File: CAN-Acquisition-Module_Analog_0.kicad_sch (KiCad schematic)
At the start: 23 parts, among them J8 OSTVN04A150, J9 OSTVN04A150, U6 BD12734FVJ-E2

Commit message: BOM updated for LCSC. Still a WIP.
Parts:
- J8, J9: LCSC (none) -> C708735; Mfr. On Shore Technology -> On-Shore
- R29, R30, R31, R32: LCSC (none) -> C351551
- R33, R34, R35, R36: Tolerance (none) -> 1%
- U6: Alternate P/N (none) -> MCP6L04T; LCSC (none) -> C49038
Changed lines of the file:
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@@
+      (effects (font (size 1.27 1.27)) hide)
+    )
+    (property "LCSC" "C351551" (id 7) (at 64.77 88.9 0)
       (effects (font (size 1.27 1.27)) hide)
     )
@@
     )
     (property "P/N" "ERA-6AEB622V" (id 6) (at 64.77 24.13 0)
+      (effects (font (size 1.27 1.27)) hide)
+    )
+    (property "LCSC" "C351551" (id 7) (at 64.77 24.13 0)
       (effects (font (size 1.27 1.27)) hide)
     )
@@
     )
     (property "P/N" "BD12734FVJ-E2" (id 5) (at 168.91 137.16 0)
+      (effects (font (size 1.27 1.27)) hide)
+    )
+    (property "Alternate P/N" "MCP6L04T" (id 6) (at 168.91 137.16 0)
+      (effects (font (size 1.27 1.27)) hide)
+    )
+    (property "LCSC" "C49038" (id 7) (at 168.91 137.16 0)
       (effects (font (size 1.27 1.27)) hide)
     )
@@
       (effects (font (size 1.27 1.27)) hide)
     )
-    (property "Mfr." "On Shore Technology" (id 5) (at 43.18 34.29 0)
+    (property "Mfr." "On-Shore" (id 5) (at 43.18 34.29 0)
+      (effects (font (size 1.27 1.27)) hide)
+    )
+    (property "LCSC" "C708735" (id 6) (at 43.18 34.29 0)
       (effects (font (size 1.27 1.27)) hide)
     )
@@
       (effects (font (size 1.27 1.27)) hide)
     )
-    (property "Mfr." "On Shore Technology" (id 5) (at 43.18 99.06 0)
+    (property "Mfr." "On-Shore" (id 5) (at 43.18 99.06 0)
+      (effects (font (size 1.27 1.27)) hide)
+    )
+    (property "LCSC" "C708735" (id 6) (at 43.18 99.06 0)
       (effects (font (size 1.27 1.27)) hide)
     )
@@
     )
     (property "P/N" "BD12734FVJ-E2" (id 5) (at 52.07 173.99 0)
+      (effects (font (size 1.27 1.27)) hide)
+    )
+    (property "Alternate P/N" "MCP6L04T" (id 6) (at 52.07 173.99 0)
+      (effects (font (size 1.27 1.27)) hide)
+    )
+    (property "LCSC" "C49038" (id 7) (at 52.07 173.99 0)
       (effects (font (size 1.27 1.27)) hide)
     )
@@
       (effects (font (size 1.27 1.27)) hide)
     )
+    (property "Alternate P/N" "MCP6L04T" (id 6) (at 168.91 69.85 0)
+      (effects (font (size 1.27 1.27)) hide)
+    )
+    (property "LCSC" "C49038" (id 7) (at 168.91 69.85 0)
+      (effects (font (size 1.27 1.27)) hide)
+    )
     (pin "1")
     (pin "2")
@@
       (effects (font (size 1.27 1.27)) hide)
     )
+    (property "Tolerance" "1%" (id 6) (at 148.59 31.75 0)
+      (effects (font (size 1.27 1.27)) hide)
+    )
     (pin "1")
     (pin "2")
@@
     )
     (property "P/N" "BD12734FVJ-E2" (id 5) (at 168.91 99.06 0)
+      (effects (font (size 1.27 1.27)) hide)
+    )
+    (property "Alternate P/N" "MCP6L04T" (id 6) (at 168.91 99.06 0)
+      (effects (font (size 1.27 1.27)) hide)
+    )
+    (property "LCSC" "C49038" (id 7) (at 168.91 99.06 0)
       (effects (font (size 1.27 1.27)) hide)
     )
@@
       (effects (font (size 1.27 1.27)) hide)
     )
+    (property "Tolerance" "1%" (id 6) (at 153.67 96.52 0)
+      (effects (font (size 1.27 1.27)) hide)
+    )
     (pin "1")
     (pin "2")
@@
     )
     (property "P/N" "ERA-6AEB622V" (id 6) (at 74.93 24.13 0)
+      (effects (font (size 1.27 1.27)) hide)
+    )
+    (property "LCSC" "C351551" (id 7) (at 74.93 24.13 0)
       (effects (font (size 1.27 1.27)) hide)
     )
@@
     )
     (property "P/N" "BD12734FVJ-E2" (id 5) (at 168.91 34.29 0)
+      (effects (font (size 1.27 1.27)) hide)
+    )
+    (property "Alternate P/N" "MCP6L04T" (id 6) (at 168.91 34.29 0)
+      (effects (font (size 1.27 1.27)) hide)
+    )
+    (property "LCSC" "C49038" (id 7) (at 168.91 34.29 0)
       (effects (font (size 1.27 1.27)) hide)
     )
@@
       (effects (font (size 1.27 1.27)) hide)
     )
+    (property "LCSC" "C351551" (id 7) (at 74.93 88.9 0)
+      (effects (font (size 1.27 1.27)) hide)
+    )
     (pin "1")
     (pin "2")
@@
       (effects (font (size 1.27 1.27)) hide)
     )
+    (property "Tolerance" "1%" (id 6) (at 144.78 101.6 0)
+      (effects (font (size 1.27 1.27)) hide)
+    )
     (pin "1")
     (pin "2")
@@
       (effects (font (size 1.27 1.27)) hide)
     )
+    (property "Tolerance" "1%" (id 6) (at 142.24 36.83 0)
+      (effects (font (size 1.27 1.27)) hide)
+    )

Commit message: BOM updated for LCSC. Still a WIP
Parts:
- D15, D16, D17, D18: LCSC (none) -> C558429
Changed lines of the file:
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@@
+      (effects (font (size 1.27 1.27)) hide)
+    )
+    (property "LCSC" "C558429" (id 6) (at 77.47 114.3 0)
       (effects (font (size 1.27 1.27)) hide)
     )
@@
     )
     (property "P/N" "D1213A-01SO-7" (id 5) (at 77.47 49.53 0)
+      (effects (font (size 1.27 1.27)) hide)
+    )
+    (property "LCSC" "C558429" (id 6) (at 77.47 49.53 0)
       (effects (font (size 1.27 1.27)) hide)
     )
@@
       (effects (font (size 1.27 1.27)) hide)
     )
+    (property "LCSC" "C558429" (id 6) (at 64.77 49.53 0)
+      (effects (font (size 1.27 1.27)) hide)
+    )
     (pin "1")
     (pin "2")
@@
       (effects (font (size 1.27 1.27)) hide)
     )
+    (property "LCSC" "C558429" (id 6) (at 64.77 114.3 0)
+      (effects (font (size 1.27 1.27)) hide)
+    )

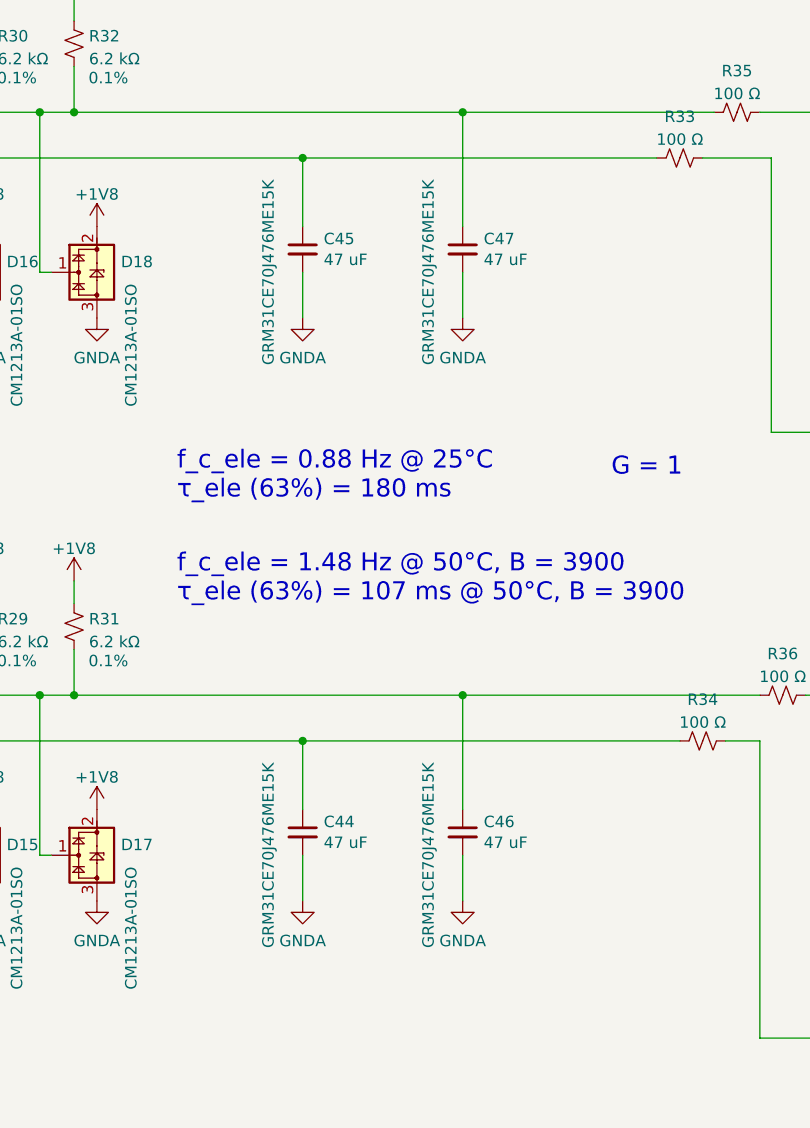
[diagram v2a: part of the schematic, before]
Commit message: Changed 47uF cap to 4.7uF
Filtration can be done in software instead of hardware
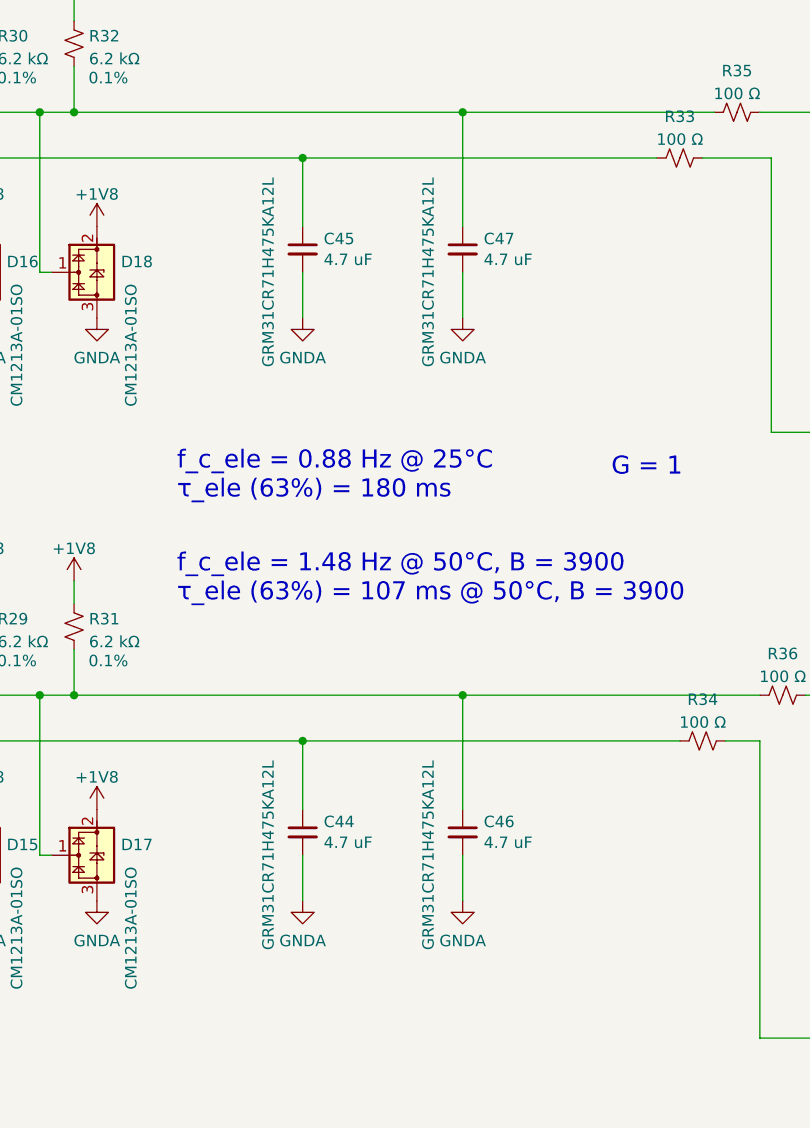
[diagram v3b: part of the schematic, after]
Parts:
- C44, C45, C46, C47: value 47 uF -> 4.7 uF; Mfr. Murata -> Murata Electronics; P/N GRM31CE70J476ME15K -> GRM31CR71H475KA12L; Rated Voltage (none) -> 50V
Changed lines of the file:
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@@
       (effects (font (size 1.27 1.27)) (justify left))
     )
-    (property "Value" "47 uF" (id 1) (at 120.4468 112.903 0)
+    (property "Value" "4.7 uF" (id 1) (at 120.4468 112.903 0)
       (effects (font (size 1.27 1.27)) (justify left))
     )
@@
       (effects (font (size 1.27 1.27)) hide)
     )
-    (property "Datasheet" "https://search.murata.co.jp/Ceramy/image/img/A01X/G101/ENG/GRM31CE70J476ME15-01.pdf" (id 3) (at 118.11 111.76 0)
-      (effects (font (size 1.27 1.27)) hide)
-    )
-    (property "P/N" "GRM31CE70J476ME15K" (id 4) (at 114.3 114.3 90))
-    (property "Mfr." "Murata" (id 5) (at 118.11 111.76 0)
+    (property "Datasheet" "https://search.murata.co.jp/Ceramy/image/img/A01X/G101/ENG/GRM31CR71H475KA12-01.pdf" (id 3) (at 118.11 111.76 0)
+      (effects (font (size 1.27 1.27)) hide)
+    )
+    (property "P/N" "GRM31CR71H475KA12L" (id 4) (at 114.3 114.3 90))
+    (property "Mfr." "Murata Electronics" (id 5) (at 118.11 111.76 0)
+      (effects (font (size 1.27 1.27)) hide)
+    )
+    (property "Rated Voltage" "50V" (id 6) (at 118.11 111.76 0)
       (effects (font (size 1.27 1.27)) hide)
     )
@@
       (effects (font (size 1.27 1.27)) (justify left))
     )
-    (property "Value" "47 uF" (id 1) (at 102.6668 112.903 0)
+    (property "Value" "4.7 uF" (id 1) (at 102.6668 112.903 0)
       (effects (font (size 1.27 1.27)) (justify left))
     )
@@
       (effects (font (size 1.27 1.27)) hide)
     )
-    (property "Datasheet" "https://search.murata.co.jp/Ceramy/image/img/A01X/G101/ENG/GRM31CE70J476ME15-01.pdf" (id 3) (at 100.33 111.76 0)
-      (effects (font (size 1.27 1.27)) hide)
-    )
-    (property "P/N" "GRM31CE70J476ME15K" (id 4) (at 96.52 114.3 90))
-    (property "Mfr." "Murata" (id 5) (at 100.33 111.76 0)
+    (property "Datasheet" "https://search.murata.co.jp/Ceramy/image/img/A01X/G101/ENG/GRM31CR71H475KA12-01.pdf" (id 3) (at 100.33 111.76 0)
+      (effects (font (size 1.27 1.27)) hide)
+    )
+    (property "P/N" "GRM31CR71H475KA12L" (id 4) (at 96.52 114.3 90))
+    (property "Mfr." "Murata Electronics" (id 5) (at 100.33 111.76 0)
+      (effects (font (size 1.27 1.27)) hide)
+    )
+    (property "Rated Voltage" "50V" (id 6) (at 100.33 111.76 0)
       (effects (font (size 1.27 1.27)) hide)
     )
@@
       (effects (font (size 1.27 1.27)) (justify left))
     )
-    (property "Value" "47 uF" (id 1) (at 120.4468 48.133 0)
+    (property "Value" "4.7 uF" (id 1) (at 120.4468 48.133 0)
       (effects (font (size 1.27 1.27)) (justify left))
     )
@@
       (effects (font (size 1.27 1.27)) hide)
     )
-    (property "Datasheet" "https://search.murata.co.jp/Ceramy/image/img/A01X/G101/ENG/GRM31CE70J476ME15-01.pdf" (id 3) (at 118.11 46.99 0)
-      (effects (font (size 1.27 1.27)) hide)
-    )
-    (property "P/N" "GRM31CE70J476ME15K" (id 4) (at 114.3 49.53 90))
-    (property "Mfr." "Murata" (id 5) (at 118.11 46.99 0)
+    (property "Datasheet" "https://search.murata.co.jp/Ceramy/image/img/A01X/G101/ENG/GRM31CR71H475KA12-01.pdf" (id 3) (at 118.11 46.99 0)
+      (effects (font (size 1.27 1.27)) hide)
+    )
+    (property "P/N" "GRM31CR71H475KA12L" (id 4) (at 114.3 49.53 90))
+    (property "Mfr." "Murata Electronics" (id 5) (at 118.11 46.99 0)
+      (effects (font (size 1.27 1.27)) hide)
+    )
+    (property "Rated Voltage" "50V" (id 6) (at 118.11 46.99 0)
       (effects (font (size 1.27 1.27)) hide)
     )
@@
       (effects (font (size 1.27 1.27)) (justify left))
     )
-    (property "Value" "47 uF" (id 1) (at 102.6668 48.133 0)
+    (property "Value" "4.7 uF" (id 1) (at 102.6668 48.133 0)
       (effects (font (size 1.27 1.27)) (justify left))
     )
@@
       (effects (font (size 1.27 1.27)) hide)
     )
-    (property "Datasheet" "https://search.murata.co.jp/Ceramy/image/img/A01X/G101/ENG/GRM31CE70J476ME15-01.pdf" (id 3) (at 100.33 46.99 0)
-      (effects (font (size 1.27 1.27)) hide)
-    )
-    (property "P/N" "GRM31CE70J476ME15K" (id 4) (at 96.52 49.53 90))
-    (property "Mfr." "Murata" (id 5) (at 100.33 46.99 0)
-      (effects (font (size 1.27 1.27)) hide)
-    )
+    (property "Datasheet" "https://search.murata.co.jp/Ceramy/image/img/A01X/G101/ENG/GRM31CR71H475KA12-01.pdf" (id 3) (at 100.33 46.99 0)
+      (effects (font (size 1.27 1.27)) hide)
+    )
+    (property "P/N" "GRM31CR71H475KA12L" (id 4) (at 96.52 49.53 90))
+    (property "Mfr." "Murata Electronics" (id 5) (at 100.33 46.99 0)
+      (effects (font (size 1.27 1.27)) hide)
+    )
+    (property "Rated Voltage" "50V" (id 6) (at 100.33 46.99 0)
+      (effects (font (size 1.27 1.27)) hide)
+    )

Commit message: Created Rev B1
Replaced buck regulator S-8581AA with AP63200 because of shortage
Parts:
- C40: LCSC P/N (none) -> C386079; LCSC Package (none) -> 0603; LCSC Specs (none) -> 1uF X7R 25V
- C41, C42, C43: LCSC P/N (none) -> C77014; LCSC Package (none) -> 0402; LCSC Specs (none) -> 100nF X7R 16V
- C44, C45, C46, C47: LCSC P/N (none) -> C92853; LCSC Package (none) -> 1206; LCSC Specs (none) -> 4.7uF X7R 50V
- D15, D16, D17, D18: LCSC C558429 -> (none); LCSC P/N (none) -> C558429; LCSC Package (none) -> SOT-23; LCSC Specs (none) -> TPCM1213A-01SO
- J8, J9: LCSC C708735 -> (none); LCSC P/N (none) -> C708735; LCSC Package (none) -> 1x4 P=2.54mm; LCSC Specs (none) -> DG308-2.54-04P-14-00A(H)
- R29, R30, R31, R32: LCSC C351551 -> (none); LCSC P/N (none) -> C351551; LCSC Package (none) -> 0805; LCSC Specs (none) -> 6K2 0.1%
- R33, R34, R35, R36: LCSC P/N (none) -> C105588; LCSC Package (none) -> 0603; LCSC Specs (none) -> 100R 1%
- U6: Alternate P/N MCP6L04T -> (none); LCSC C49038 -> (none); LCSC P/N (none) -> C693071; LCSC Package (none) -> TSSOP-14; LCSC Specs (none) -> COS6004TR

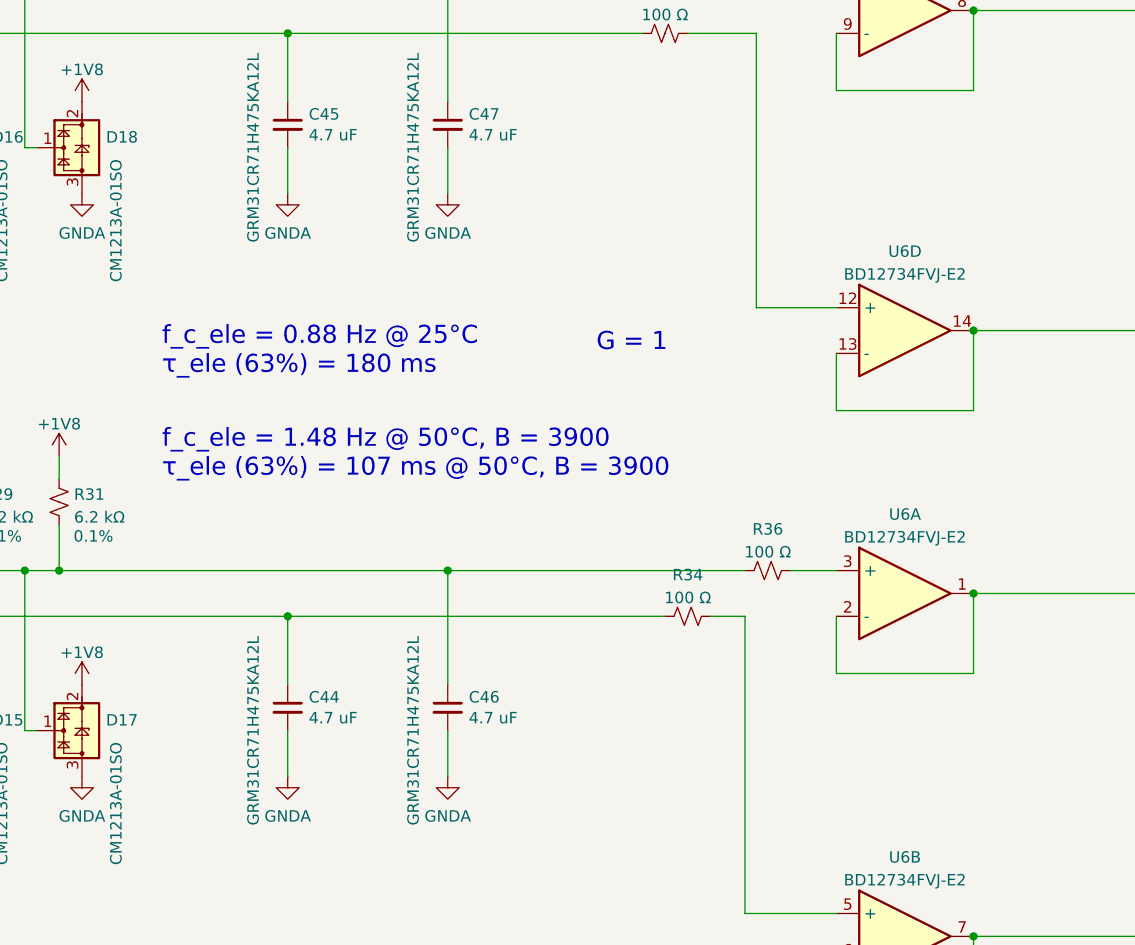
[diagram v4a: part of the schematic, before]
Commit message: Created rev B2 to fix low pass filter specs
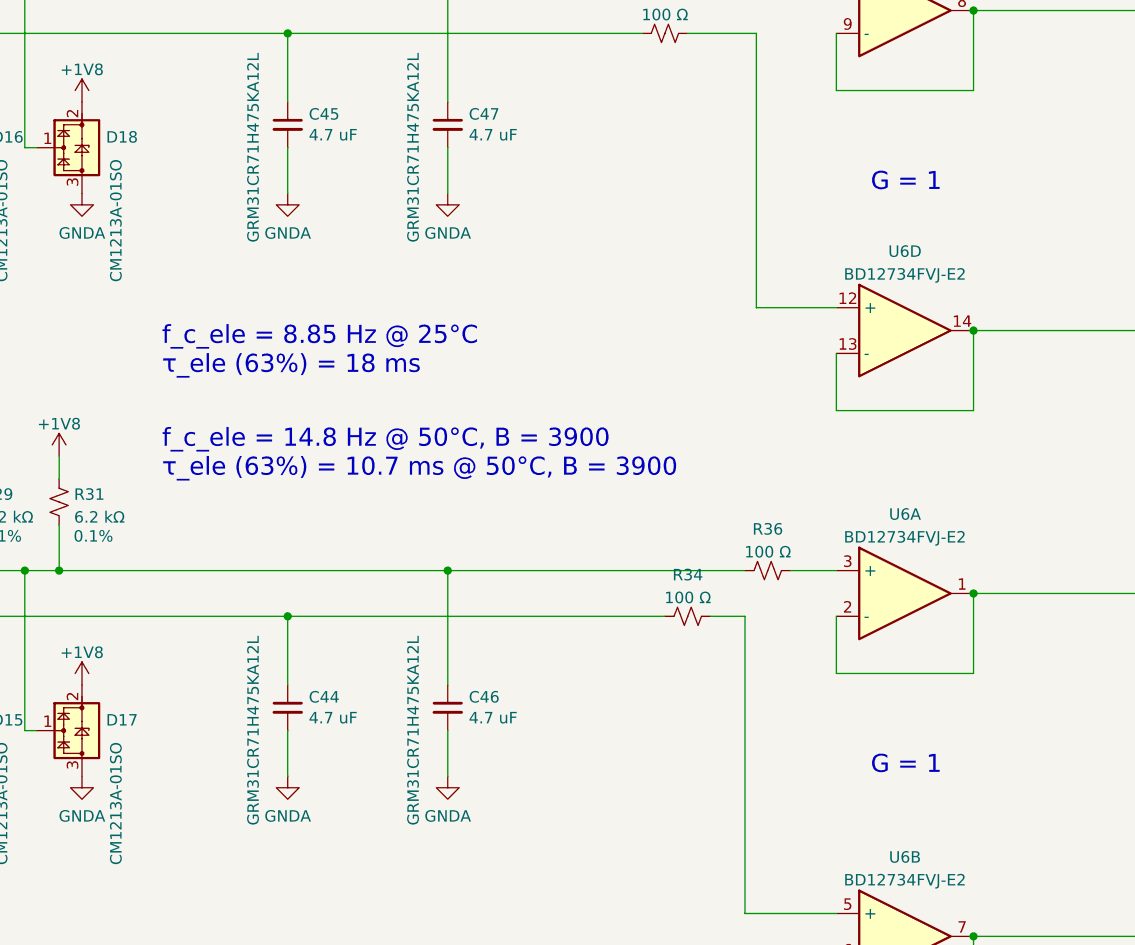
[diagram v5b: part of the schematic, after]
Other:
- note added: "f_c_ele = 14.8 Hz @ 50°C, B = 3900 τ_ele (63%) = 10.7 ms @ 50°C, B = 3900"
- note added: "f_c_ele = 8.85 Hz @ 25°C τ_ele (63%) = 18 ms"
- note removed: "f_c_ele = 0.88 Hz @ 25°C τ_ele (63%) = 180 ms"
- note removed: "f_c_ele = 1.48 Hz @ 50°C, B = 3900 τ_ele (63%) = 107 ms @ 50°C, B = 3900"
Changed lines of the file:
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@@
     (effects (font (size 2 2)) (justify left bottom))
   )
-  (text "f_c_ele = 1.48 Hz @ 50°C, B = 3900\nτ_ele (63%) = 107 ms @ 50°C, B = 3900"
+  (text "f_c_ele = 14.8 Hz @ 50°C, B = 3900\nτ_ele (63%) = 10.7 ms @ 50°C, B = 3900"
     (at 86.36 86.36 0)
     (effects (font (size 2 2)) (justify left bottom))
   )
-  (text "G = 1" (at 134.62 72.39 0)
+  (text "G = 1" (at 165.1 54.61 0)
     (effects (font (size 2 2)) (justify left bottom))
   )
-  (text "f_c_ele = 0.88 Hz @ 25°C\nτ_ele (63%) = 180 ms" (at 86.36 74.93 0)
+  (text "G = 1" (at 165.1 119.38 0)
     (effects (font (size 2 2)) (justify left bottom))
   )
+  (text "f_c_ele = 8.85 Hz @ 25°C\nτ_ele (63%) = 18 ms" (at 86.36 74.93 0)
+    (effects (font (size 2 2)) (justify left bottom))
+  )
